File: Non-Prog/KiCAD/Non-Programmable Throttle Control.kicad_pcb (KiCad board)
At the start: 2 copper layers, 20 x 20 mm, 13 parts

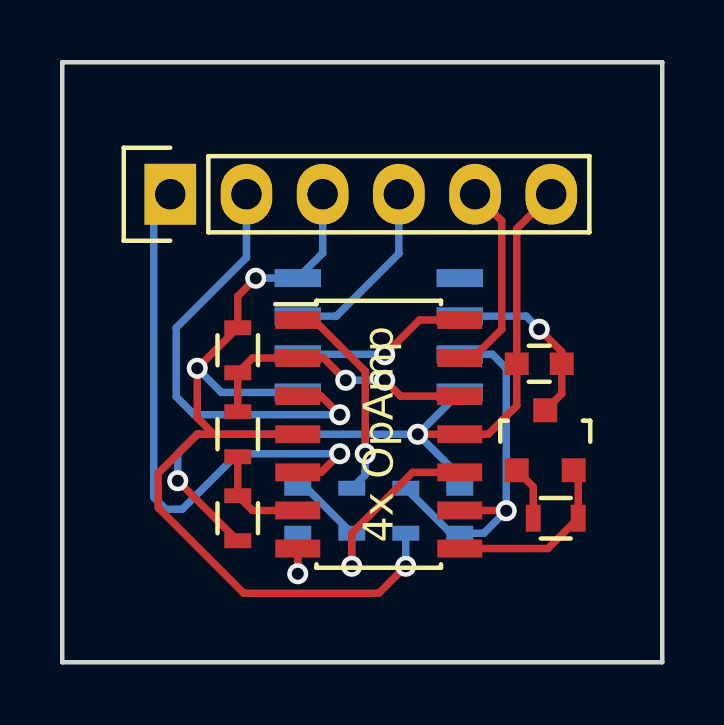
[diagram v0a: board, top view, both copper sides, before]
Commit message: Updated Details, Added pinout to schematic
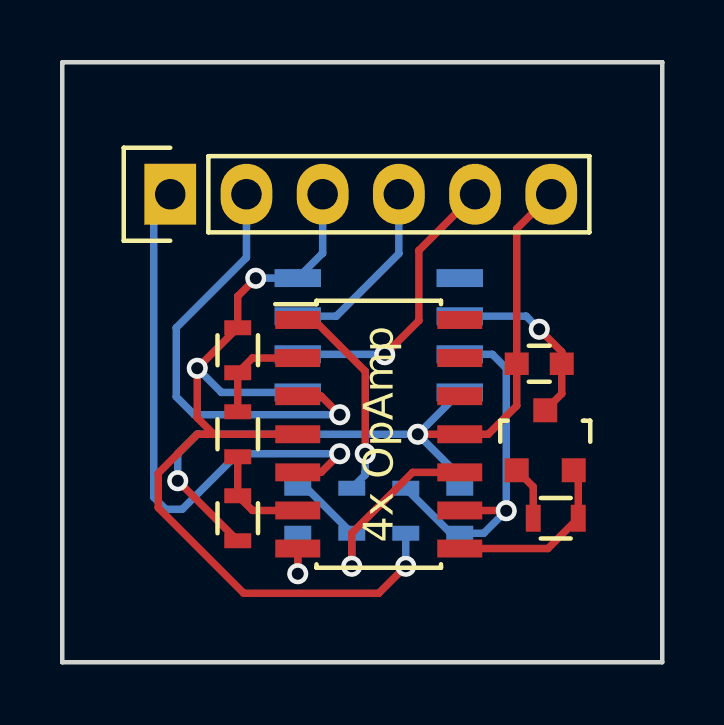
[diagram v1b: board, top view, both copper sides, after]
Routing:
- net (no net): track 169.7 -> 160.7 mm, vias 15 -> 13
- added copper zone on B.Cu, net (none)
- added copper zone on F.Cu, net (none)
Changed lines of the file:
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@@
     (thickness 1.6)
     (drawings 4)
-    (tracks 124)
+    (tracks 114)
     (zones 0)
     (modules 13)
@@
     (visible_elements 7FFFFF7F)
     (pcbplotparams
-      (layerselection 0x010f0_80000001)
+      (layerselection 0x01000_00000000)
       (usegerberextensions false)
       (excludeedgelayer true)
@@
   (gr_line (start 145.5 68.35) (end 145.5 88.35) (angle 90) (layer Edge.Cuts) (width 0.15))
   (gr_line (start 125.5 68.35) (end 145.5 68.35) (angle 90) (layer Edge.Cuts) (width 0.15))
-  (segment (start 138.75 78.21) (end 139.19 78.21) (width 0.25) (layer F.Cu) (net 0))
-  (segment (start 139.19 78.21) (end 140.15 77.25) (width 0.25) (layer F.Cu) (net 0))
-  (segment (start 140.15 77.25) (end 140.15 73.64) (width 0.25) (layer F.Cu) (net 0))
-  (segment (start 140.15 73.64) (end 139.26 72.75) (width 0.25) (layer F.Cu) (net 0))
+  (segment (start 137.3875 76.9625) (end 137.3875 74.6225) (width 0.25) (layer F.Cu) (net 0))
+  (segment (start 137.3875 74.6225) (end 139.26 72.75) (width 0.25) (layer F.Cu) (net 0))
   (segment (start 140.65 78.4) (end 140.65 73.9) (width 0.25) (layer F.Cu) (net 0))
   (segment (start 140.65 73.9) (end 141.8 72.75) (width 0.25) (layer F.Cu) (net 0))
   (segment (start 133.35 78.085) (end 136.235 78.085) (width 0.25) (layer B.Cu) (net 0))
-  (segment (start 137.41 76.94) (end 138.75 76.94) (width 0.25) (layer F.Cu) (net 0))
-  (segment (start 136.25 78.1) (end 137.41 76.94) (width 0.25) (layer F.Cu) (net 0))
+  (segment (start 136.235 78.085) (end 136.25 78.1) (width 0.25) (layer B.Cu) (net 0))
   (via (at 136.25 78.1) (size 0.7) (drill 0.4) (layers F.Cu B.Cu) (net 0))
-  (segment (start 136.235 78.085) (end 136.25 78.1) (width 0.25) (layer B.Cu) (net 0))
+  (segment (start 136.25 78.1) (end 137.3875 76.9625) (width 0.25) (layer F.Cu) (net 0))
   (segment (start 131.35 81.4) (end 129.5 83.25) (width 0.25) (layer B.Cu) (net 0))
   (segment (start 128.55 82.85) (end 128.55 73.3) (width 0.25) (layer B.Cu) (net 0))
@@
   (segment (start 140.65 79.8) (end 140.65 78.4) (width 0.25) (layer F.Cu) (net 0))
   (segment (start 139.7 80.75) (end 140.65 79.8) (width 0.25) (layer F.Cu) (net 0))
-  (segment (start 138.75 79.48) (end 136.78 79.48) (width 0.25) (layer F.Cu) (net 0))
-  (segment (start 134.21 78.21) (end 134.95 78.95) (width 0.25) (layer F.Cu) (net 0))
-  (via (at 134.95 78.95) (size 0.7) (drill 0.4) (layers F.Cu B.Cu) (net 0))
-  (segment (start 134.95 78.95) (end 136.25 78.95) (width 0.25) (layer B.Cu) (net 0))
-  (via (at 136.25 78.95) (size 0.7) (drill 0.4) (layers F.Cu B.Cu) (net 0))
-  (segment (start 134.21 78.21) (end 133.35 78.21) (width 0.25) (layer F.Cu) (net 0))
-  (segment (start 136.78 79.48) (end 136.25 78.95) (width 0.25) (layer F.Cu) (net 0))
   (segment (start 133.89 76.94) (end 135.6 78.65) (width 0.25) (layer F.Cu) (net 0))
   (segment (start 135.6 82.1) (end 135.15 82.55) (width 0.25) (layer B.Cu) (net 0))
@@
   (segment (start 131.35 82.8) (end 131.35 81.5) (width 0.25) (layer F.Cu) (net 0))
   (segment (start 131.35 80) (end 131.35 78.7) (width 0.25) (layer F.Cu) (net 0))
+  (zone (net 0) (net_name "") (layer F.Cu) (hatch edge 0.508)
+    (connect_pads (clearance 0.508))
+    (min_thickness 0.254)
+    (fill yes (arc_segments 16) (thermal_gap 0.508) (thermal_bridge_width 0.508))
+    (polygon
+      (pts
+        (xy 125.475 68.325) (xy 145.475 68.35) (xy 145.5 88.325) (xy 125.525 88.35)
+      )
+    )
+  )
+  (zone (net 0) (net_name "") (layer B.Cu) (hatch edge 0.508)
+    (connect_pads (clearance 0.508))
+    (min_thickness 0.254)
+    (fill yes (arc_segments 16) (thermal_gap 0.508) (thermal_bridge_width 0.508))
+    (polygon
+      (pts
+        (xy 125.5 68.35) (xy 145.5 68.375) (xy 145.5 88.35) (xy 125.525 88.35)
+      )
+    )
+  )
 )
